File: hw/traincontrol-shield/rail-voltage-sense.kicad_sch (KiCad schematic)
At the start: 2 parts

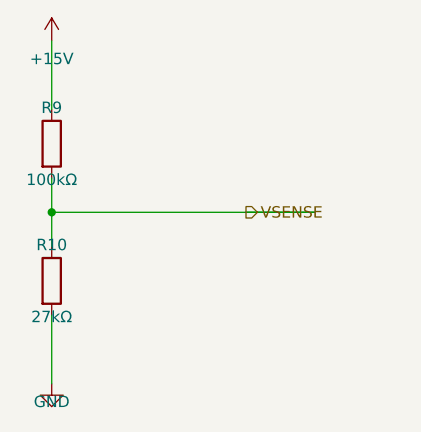
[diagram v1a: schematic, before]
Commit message: Fix hierarchical label placement and orientation in sub-sheets
Root cause: hlabel() placed the label at lx (stub tip) instead of x
(circuit connection point), mirroring the Issue-2 glabel bug fixed in
commit 2270223.

Fix applied to hlabel():
  (at {lx} ...) → (at {x} ...)  — label now sits at the circuit endpoint

Angle convention (matches label body direction):
  angle=180 → body extends LEFT  — left-side input/bidirectional labels
  angle=0   → body extends RIGHT — right-side output/bidirectional labels

Sheets affected: zero-crossing, xor-interlock, opto-triac-drive,
rail-voltage-sense; triacs-snubbers and mcu already had correct angles.

Co-Authored-By: Claude Sonnet 4.6 <noreply@anthropic.com>
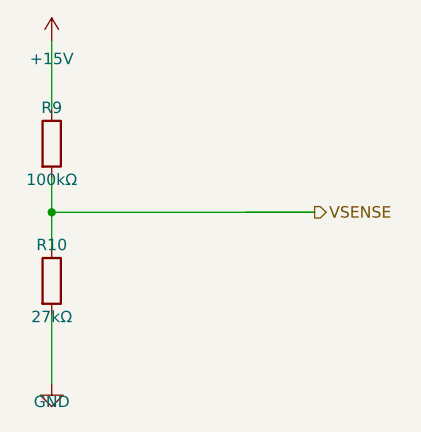
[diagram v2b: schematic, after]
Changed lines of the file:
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@@
 	(hierarchical_label "VSENSE"
 		(shape output)
-		(at 101.6 83.82 0)
+		(at 109.22 83.82 0)
 		(fields_autoplaced yes)
 		(effects (font (size 1.27 1.27)) (justify left bottom))
 		(property "Intersheetrefs" "${INTERSHEET_REFS}"
-			(at 101.6 83.82 0)
+			(at 109.22 83.82 0)
 			(effects (font (size 1.27 1.27)) (hide yes))
 		)

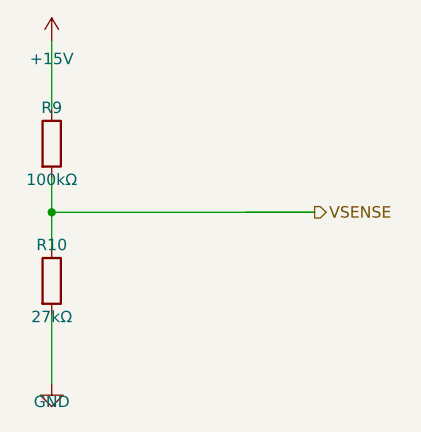
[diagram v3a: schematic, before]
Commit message: Fix hlabel stub direction: stubs now extend away from IC, not into it
Root cause: hlabel() used dx = +STUB for angle=180 and -STUB for angle=0,
which caused every stub wire to run INTO the IC body instead of outward.
This made wires appear to connect at the inner (wrong) end of all pins.

Fix: negate dx so stubs always extend outward from the pin tip:
  angle=180 (left-side input):  dx = -STUB → stub extends LEFT  ✓
  angle=0   (right-side output): dx = +STUB → stub extends RIGHT ✓

Also revert the x-position workarounds that compensated for the wrong
stub direction (zero-crossing AC_IN, opto-triac PHASE/GATE, power-supply
AC_IN/RTN): these are now back at the actual component pin positions.

All 8 sheets validate with kicad-cli.

Co-Authored-By: Claude Sonnet 4.6 <noreply@anthropic.com>
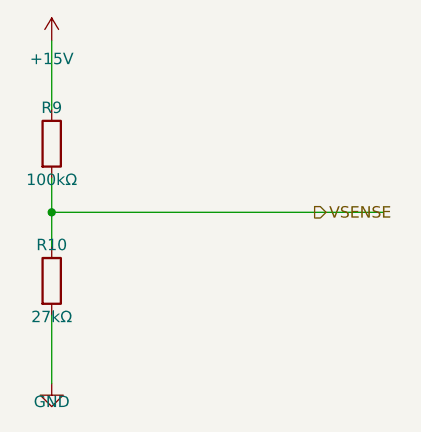
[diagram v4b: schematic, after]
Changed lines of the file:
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@@
 	)
 	(wire
-		(pts (xy 101.6 83.82) (xy 109.22 83.82))
+		(pts (xy 109.22 83.82) (xy 116.84 83.82))
 		(stroke (width 0) (type solid))
 	)
